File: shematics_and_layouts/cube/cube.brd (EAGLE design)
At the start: 160 x 100 mm, 23 parts, among them K1 LD1117AV33, X1 LEDs

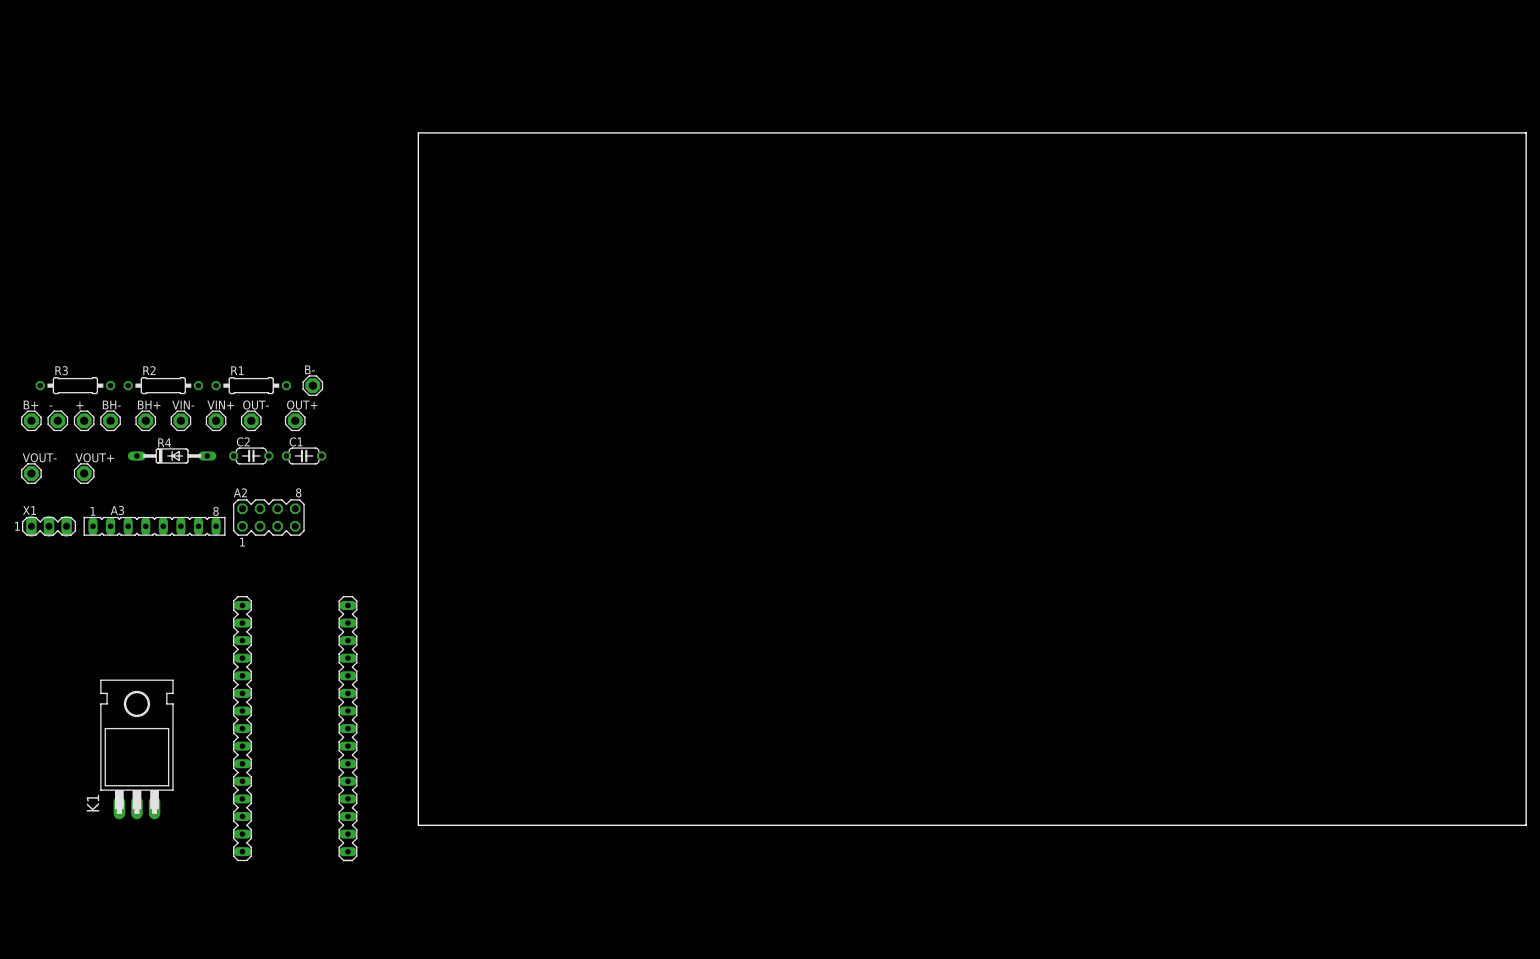
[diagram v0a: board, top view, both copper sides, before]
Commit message: TASK: Board outlines for U-Suply components
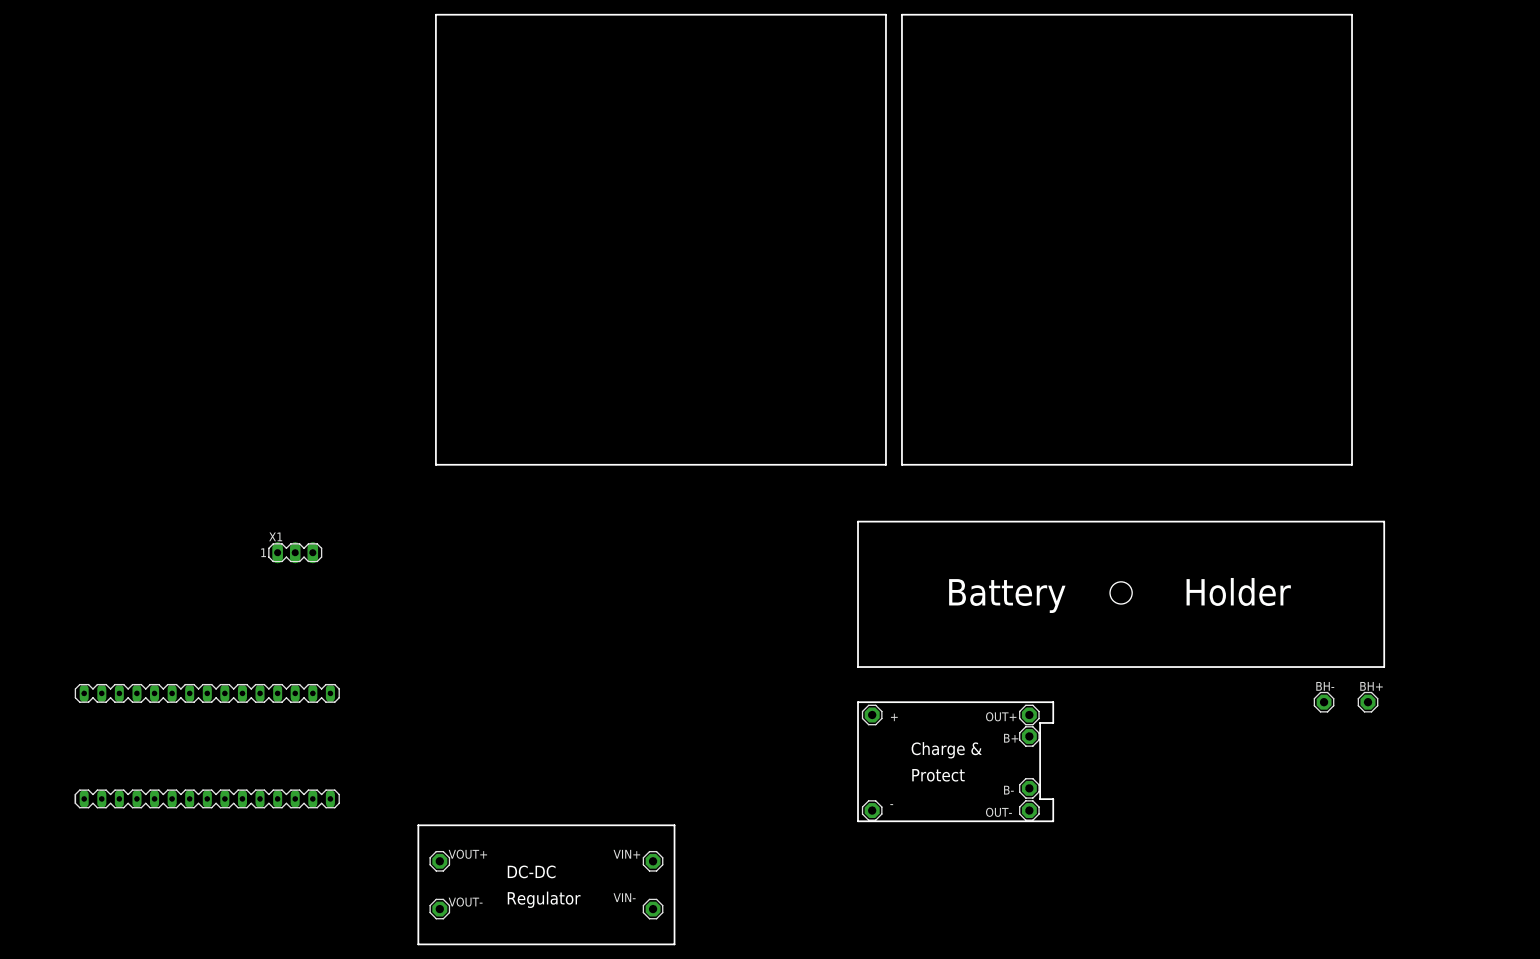
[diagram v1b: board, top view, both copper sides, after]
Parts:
- removed A2: ESP8266, con-lstb:MA04-2
- removed A3: MPU-6050, con-lsta:FE08
- removed C1, C2: 100n, rcl:C050-024X044
- removed K1: LD1117AV33, linear:TO220H
- removed R1: 10K, rcl:0207/10
- removed R2: 1K, rcl:0207/10
- removed R3: 2K, rcl:0207/10
- removed R4: RGP10M, diode:DO35-10
- moved BH+ 181.1 mm to (137.2, 17.8)
- moved BH- 179.9 mm to (130.8, 17.8)
- moved B+ 151.2 mm to (88.2, 12.8)
- moved - 130.4 mm to (65.5, 2.13)
- moved OUT- 125.7 mm to (88.2, 2.13)
- moved + 121.5 mm to (65.5, 15.9)
- moved B- 118.7 mm to (88.2, 5.33)
- moved OUT+ 114.2 mm to (88.2, 15.9)
- moved VIN- 98.1 mm to (33.9, -12.1)
- moved VIN+ 89.6 mm to (33.9, -5.20)
- moved VOUT- 86.2 mm to (3.10, -12.1)
- moved VOUT+ 76.0 mm to (3.10, -5.20)
- moved X1 35.8 mm to (-17.8, 39.4)
- moved A1 24.4 mm to (-39.4, 8.89), turned to 270 degrees
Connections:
- removed net N$10: A1.A4, A3.4
- removed net N$11: A1.A5, A3.3
- removed net N$3: A2.2, C2.1, K1.3, R1.1, R4.A
- removed net N$4: A2.1, R2.2, R3.1
- removed net N$5: A2.6, R1.2
- removed net N$6: A1.D2, A2.8
- removed net N$8: A1.D3, R2.1
- net GND: no longer A2.7, A3.2, C1.2, C2.2, K1.2, R3.2
- net VCC: now also A1.RAW; no longer A1.5V, A3.1, C1.1, K1.1, R4.C
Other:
- board size 160 x 100 mm -> 139.5 x 134.3 mm
- board text added: "Battery"
- board text added: "Charge &"
- board text added: "DC-DC"
- board text added: "Holder"
- board text added: "Protect"
- board text added: "Regulator"
